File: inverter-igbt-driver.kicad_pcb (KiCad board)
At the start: 2 copper layers, 84.5 x 64 mm, 68 parts, among them J1 CONTROL, U1 NE555, U2 IXDF604SIA, U3 FOD8316, U5 FOD8316, U6 Transformer_2P_2S, U8 Transformer_2P_2S, U9 IGBT_HALF_BRIDGE

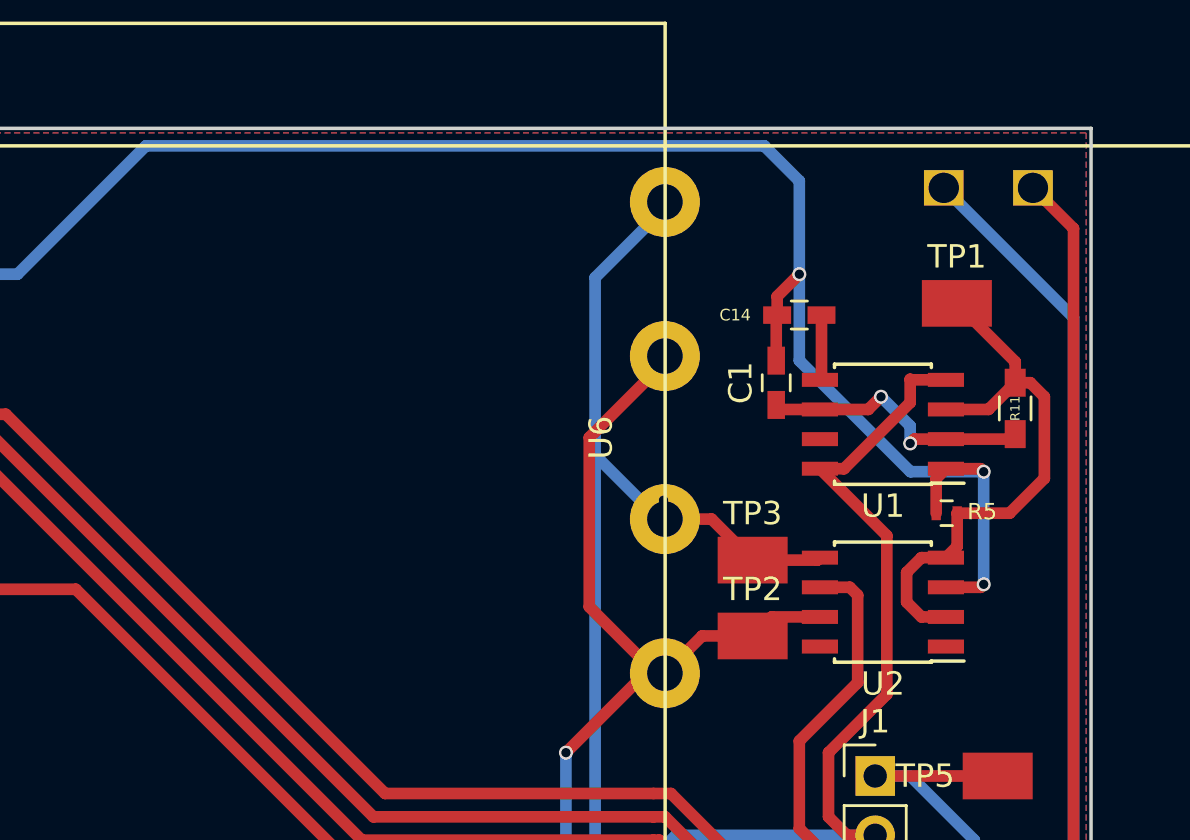
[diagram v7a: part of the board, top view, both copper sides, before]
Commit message: Adding d-flop to achieve 50% duty cycle
555 timer config cannot guarantee 50% duty cycle, but a frequency divider can.
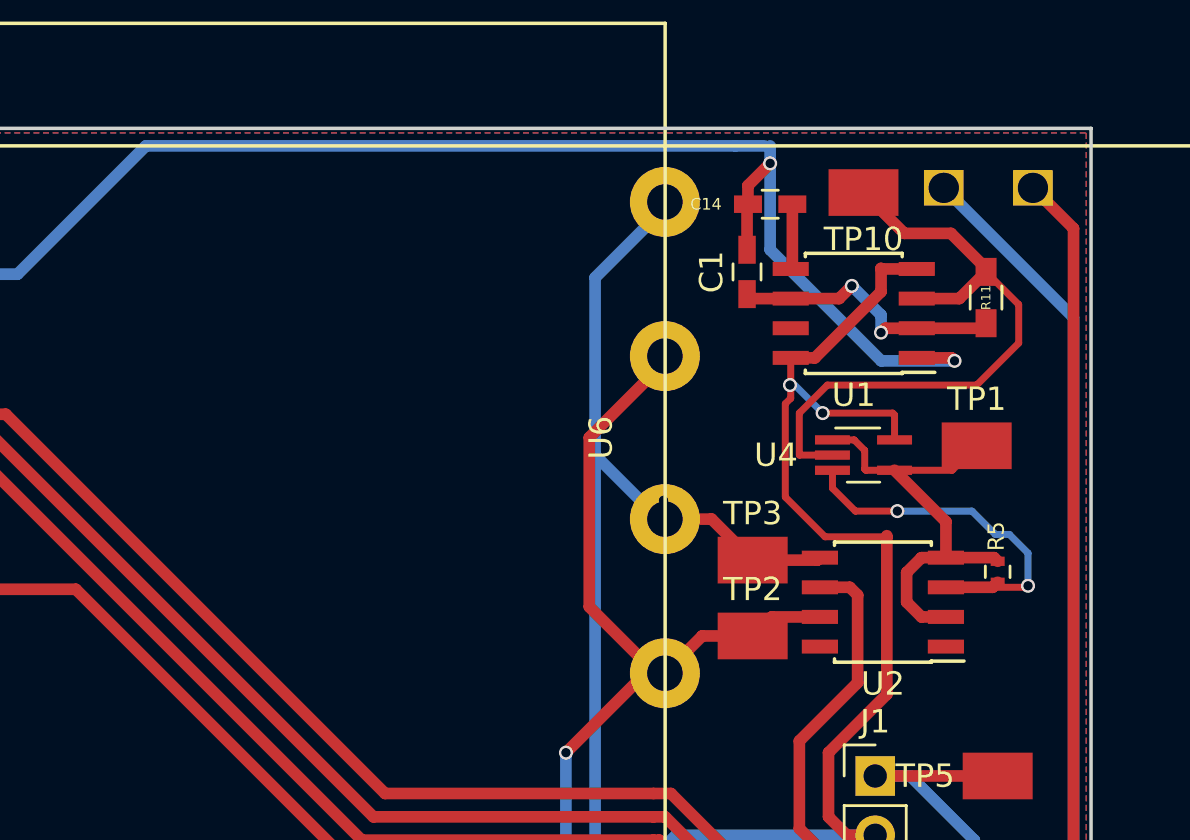
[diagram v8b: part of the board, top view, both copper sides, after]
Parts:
- added TP10: TEST, inverter-igbt-driver:TP RCT (0805), F.Cu at (167.8, 23.8)
- added U4: 74LVC1G80GV, TO_SOT_Packages_SMD:SOT-353_SC-70-5_Handsoldering, F.Cu at (167.8, 35.0)
- moved TP1 6.16 mm to (172.6, 34.6)
- moved C1 4.91 mm to (162.8, 27.2)
- moved C14 4.91 mm to (163.8, 24.2)
- moved R11 4.91 mm to (173.0, 28.2)
- moved U1 4.91 mm to (167.3, 28.9)
- moved R5 3.33 mm to (173.5, 40.0), turned to 270 degrees
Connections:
- R5 pad 1: Net-(R11-Pad2) -> Net-(R5-Pad1)
- TP1 pad 1: Net-(R11-Pad2) -> Net-(R5-Pad1)
- U2 pad 2: Net-(R11-Pad2) -> Net-(R5-Pad1)
- U2 pad 4: Net-(R11-Pad2) -> Net-(R5-Pad1)
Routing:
- net Net-(R5-Pad1): track 0.00 -> 19.7 mm
- net +5V: track 149.1 -> 162.3 mm, vias 1 -> 3
- net Net-(R11-Pad2): track 24.5 -> 27.7 mm
- net GND: track 167.6 -> 169.2 mm, vias 12 -> 13
